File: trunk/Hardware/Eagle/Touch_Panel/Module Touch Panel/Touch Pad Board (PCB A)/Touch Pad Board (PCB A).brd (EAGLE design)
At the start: 140.7 x 94.5 mm, 50 parts, among them U1 SCT2024(CSOG,CSSG,CSTG,CSDG), U2 SCT2024(CSOG,CSSG,CSTG,CSDG), X0 TPTP10R, X1 TPTP10R, X2 TPTP10R, X3 TPTP10R, X4 TPTP10R, Y0 TPTP10R, Y1 TPTP10R, Y2 TPTP10R

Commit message: Work in progress
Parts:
- removed X0, X1, X2, X3, X4, Y0, Y1, Y2: TPTP10R, testpad:TP10R
- moved LED6 77.2 mm to (84.8, 8.99)
- moved LED7 77.0 mm to (109.1, 8.95)
- moved LED12 72.9 mm to (11.9, 59.5), turned to 0 degrees
- moved LED15 72.9 mm to (84.8, 59.5), turned to 0 degrees
- moved LED5 48.6 mm to (60.6, 8.98)
- moved LED4 48.6 mm to (36.2, 9.14)
- moved LED3 34.9 mm to (36.3, 34.0)
- moved LED1 24.9 mm to (11.8, 33.9), turned to 0 degrees
- moved LED2 24.4 mm to (11.8, 9.02)
- moved LED14 24.3 mm to (60.5, 59.5), turned to 0 degrees
- moved LED13 24.3 mm to (36.2, 59.5), turned to 0 degrees
- moved C2 15.6 mm to (58.3, 22.1)
- moved R1 15.0 mm to (58.4, 26.2)
- moved R4 14.1 mm to (58.3, 24.1)
- moved LED26 10.2 mm to (52.1, 20.6)
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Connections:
- removed net N$16: JP2.4, Y1.TP
- removed net N$41: JP2.3, Y0.TP
- removed net N$42: JP3.4, Y2.TP
- removed net N$44: JP4.4, X1.TP
- removed net N$45: JP4.3, X2.TP
- removed net N$46: JP4.2, X0.TP
- removed net N$48: JP5.2, X3.TP
- removed net N$51: JP5.4, X4.TP
- new net X0: JP4.2
- new net X1: JP4.4
- new net X2: JP4.3
- new net X3: JP5.2
- new net X4: JP5.4
- new net Y0: JP2.3
- new net Y1: JP2.4
- new net Y2: JP3.4
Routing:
- net Y2: track 0.00 -> 280.4 mm
- net Y0: track 0.00 -> 279.9 mm
- net Y1: track 0.00 -> 278.8 mm
- net N$29: track 0.00 -> 178.4 mm
- net N$30: track 0.00 -> 150.4 mm
- net N$1: track 0.00 -> 132.5 mm
- net N$31: track 0.00 -> 122.6 mm
- net N$9: track 0.00 -> 109.3 mm
- net N$3: track 0.00 -> 107.1 mm
- net N$2: track 0.00 -> 106.0 mm
- net N$32: track 0.00 -> 94.3 mm
- net N$4: track 0.00 -> 79.3 mm
- net N$8: track 0.00 -> 74.0 mm
- net N$5: track 0.00 -> 52.4 mm
- net N$28: track 0.00 -> 51.7 mm
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- added copper zone on layer 16, net X0
- added copper zone on layer 16, net X1
- added copper zone on layer 16, net X2
- added copper zone on layer 16, net X3
- added copper zone on layer 16, net X4
- removed copper zone on layer 16, net 1B1
- removed copper zone on layer 16, net 1B10
- removed copper zone on layer 16, net 1B11
- removed copper zone on layer 16, net 1B12
- removed copper zone on layer 16, net 1B13
- removed copper zone on layer 16, net 1B14
- removed copper zone on layer 16, net 1B15
- removed copper zone on layer 16, net 1B2
- removed copper zone on layer 16, net 1B3
- removed copper zone on layer 16, net 1B4
- removed copper zone on layer 16, net 1B5
- removed copper zone on layer 16, net 1B6
- removed copper zone on layer 16, net 1B7
- removed copper zone on layer 16, net 1B8
- removed copper zone on layer 16, net 1B9
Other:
- outline, holes or cut-outs redrawn

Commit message: Board of TPB (PCB A) - :)Done
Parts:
- moved JP3 26.6 mm to (71.5, 53.5)
- moved JP2 26.6 mm to (63.7, 28.2)
- moved D1 3.30 mm to (84.8, 53.3), turned to 270 degrees
- moved C2 2.10 mm to (58.3, 24.2)
- moved R4 1.98 mm to (58.3, 22.1)
- moved JP4 0.80 mm to (63.8, 53.5)
- moved JP1 0.16 mm to (80.7, 41.4)
- turned LED10 to 180 degrees
- turned LED5 to 180 degrees
- turned LED8 to 180 degrees
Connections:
- net GND: now also JP2.3, JP2.4, JP3.2; no longer JP2.1, JP2.2, JP3.3
- net Y0: now also JP2.2; no longer JP2.3
- net Y1: now also JP2.1; no longer JP2.4
- net Y2: now also JP3.3; no longer JP3.4
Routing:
- net LED_DP: track 0.00 -> 386.7 mm, vias 0 -> 21
- net +3V3: track 0.00 -> 114.4 mm, vias 0 -> 9
- net GND: track 11.4 -> 110.2 mm, vias 0 -> 7
- net N$36: track 0.00 -> 62.2 mm, vias 0 -> 3
- net N$35: track 0.00 -> 61.7 mm, vias 0 -> 3
- net N$34: track 10.7 -> 69.8 mm, vias 0 -> 4
- net X4: track 40.0 -> 94.6 mm
- net N$8: track 74.0 -> 25.8 mm, vias 0 -> 2
- net X0: track 34.0 -> 78.0 mm, vias 0 -> 2
- net X1: track 35.9 -> 68.5 mm
- net Y0: track 279.9 -> 308.8 mm, vias 0 -> 1
- net N$37: track 0.00 -> 19.9 mm, vias 0 -> 2
- net X3: track 34.4 -> 50.8 mm
- net 1: track 16.1 -> 0.00 mm
- net N$5: track 52.4 -> 44.4 mm
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- added copper zone on layer 1, net N$14
- removed copper zone on layer 16, net 1B
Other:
- board size 140.7 x 94.5 mm -> 142.3 x 82 mm
- board text added: "Touch Pad Board (PCB A) ver. 1.00"

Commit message: Work in progress
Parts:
- added R5: 10, resistor:R0805
- added U$1: PHOTO_TRANS, myHome:PHOTO_TRANS
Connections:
- new net N$15: JP3.1, R5.2, U$1.C
- net +3V3: now also U$1.A
- net GND: now also R5.1; no longer JP3.1
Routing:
- net X2: track 37.0 -> 51.7 mm
- net +3V3: track 114.4 -> 123.1 mm, vias 9 -> 10
- net N$15: track 0.00 -> 7.02 mm
- net GND: track 110.2 -> 107.4 mm
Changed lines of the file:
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@@
 <layer number="17" name="Pads" color="2" fill="1" visible="yes" active="yes"/>
 <layer number="18" name="Vias" color="2" fill="1" visible="yes" active="yes"/>
-<layer number="19" name="Unrouted" color="6" fill="1" visible="no" active="yes"/>
-<layer number="20" name="Dimension" color="15" fill="1" visible="yes" active="yes"/>
+<layer number="19" name="Unrouted" color="6" fill="1" visible="yes" active="yes"/>
+<layer number="20" name="Dimension" color="15" fill="1" visible="no" active="yes"/>
 <layer number="21" name="tPlace" color="7" fill="1" visible="no" active="yes"/>
 <layer number="22" name="bPlace" color="7" fill="1" visible="no" active="yes"/>
 <layer number="23" name="tOrigins" color="15" fill="1" visible="no" active="yes"/>
 <layer number="24" name="bOrigins" color="15" fill="1" visible="no" active="yes"/>
-<layer number="25" name="tNames" color="7" fill="1" visible="yes" active="yes"/>
-<layer number="26" name="bNames" color="7" fill="1" visible="yes" active="yes"/>
+<layer number="25" name="tNames" color="7" fill="1" visible="no" active="yes"/>
+<layer number="26" name="bNames" color="7" fill="1" visible="no" active="yes"/>
 <layer number="27" name="tValues" color="7" fill="1" visible="no" active="yes"/>
 <layer number="28" name="bValues" color="7" fill="1" visible="no" active="yes"/>
@@
 <layer number="37" name="tTest" color="7" fill="1" visible="no" active="yes"/>
 <layer number="38" name="bTest" color="7" fill="1" visible="no" active="yes"/>
-<layer number="39" name="tKeepout" color="4" fill="11" visible="no" active="yes"/>
-<layer number="40" name="bKeepout" color="1" fill="11" visible="no" active="yes"/>
-<layer number="41" name="tRestrict" color="4" fill="10" visible="no" active="yes"/>
-<layer number="42" name="bRestrict" color="1" fill="10" visible="no" active="yes"/>
+<layer number="39" name="tKeepout" color="4" fill="11" visible="yes" active="yes"/>
+<layer number="40" name="bKeepout" color="1" fill="11" visible="yes" active="yes"/>
+<layer number="41" name="tRestrict" color="4" fill="10" visible="yes" active="yes"/>
+<layer number="42" name="bRestrict" color="1" fill="10" visible="yes" active="yes"/>
 <layer number="43" name="vRestrict" color="2" fill="10" visible="no" active="yes"/>
 <layer number="44" name="Drills" color="7" fill="1" visible="no" active="yes"/>
-<layer number="45" name="Holes" color="7" fill="1" visible="yes" active="yes"/>
+<layer number="45" name="Holes" color="7" fill="1" visible="no" active="yes"/>
 <layer number="46" name="Milling" color="3" fill="1" visible="no" active="yes"/>
 <layer number="47" name="Measures" color="7" fill="1" visible="no" active="yes"/>
@@
 <rectangle x1="98.38" y1="13.61" x2="111.87" y2="18.01" layer="41"/>
 <rectangle x1="73.96" y1="38.65" x2="87.45" y2="43.05" layer="41"/>
-<rectangle x1="57.84" y1="17.29" x2="71.33" y2="21.69" layer="41" rot="R90"/>
+<rectangle x1="57.84" y1="18.19" x2="71.33" y2="22.59" layer="41" rot="R90"/>
 <rectangle x1="57.63" y1="34.56" x2="71.12" y2="38.96" layer="41" rot="R90"/>
-<rectangle x1="65.83" y1="59.96" x2="79.32" y2="64.36" layer="41" rot="R90"/>
+<rectangle x1="65.93" y1="58.66" x2="79.42" y2="63.06" layer="41" rot="R90"/>
 <text x="130.5" y="2.55" size="1.778" layer="16" rot="MR0">Touch Pad Board (PCB A) ver. 1.00</text>
 <rectangle x1="25.44" y1="64.32" x2="38.93" y2="68.72" layer="42"/>
 <text x="91.44" y="2.54" size="1.778" layer="25">Touch Pad Board (PCB A) ver. 1.00</text>
 <text x="91.54" y="4.26" size="1.778" layer="26" rot="MR180">Touch Pad Board (PCB A) ver. 1.00</text>
-<hole x="77.47" y="53.34" drill="0.6"/>
 </plain>
 <attributes>
@@
 <element name="JP5" library="pinhead" package="2X2SMD" value="" x="73.54" y="28.18" locked="yes" rot="MR0"/>
 <element name="JP1" library="pinhead" package="2X3SMD" value="" x="80.72" y="41.41" locked="yes" rot="MR90"/>
+<element name="U$1" library="myHome" package="PHOTO_TRANS" value="PHOTO_TRANS" x="68.57" y="54.01" rot="MR180"/>
+<element name="R5" library="resistor" package="R0805" value="10" x="68.66" y="50.43" rot="MR90"/>
 </elements>
 <signals>
@@
 <contactref element="C2" pad="1"/>
 <contactref element="C1" pad="1"/>
-<contactref element="JP3" pad="1"/>
 <contactref element="JP1" pad="P1"/>
 <wire x1="54.15" y1="26.2225" x2="55.3225" y2="26.2225" width="0.3048" layer="16"/>
@@
 <wire x1="65.615" y1="25.65" x2="65.615" y2="23.015" width="0.6096" layer="16"/>
 <wire x1="65.615" y1="23.015" x2="65.4" y2="22.8" width="0.6096" layer="16"/>
-<wire x1="70.915" y1="56.06" x2="70.915" y2="50.98" width="0.6096" layer="16"/>
 <wire x1="77.545" y1="38.235" x2="77.51" y2="38.2" width="0.6096" layer="16"/>
 <wire x1="77.51" y1="38.2" x2="76.2" y2="38.2" width="0.6096" layer="16"/>
@@
 <wire x1="75" y1="48.3" x2="71.2" y2="48.3" width="0.6096" layer="16"/>
 <wire x1="71.2" y1="48.3" x2="71" y2="48.5" width="0.6096" layer="16"/>
-<wire x1="71" y1="48.5" x2="71" y2="50.68" width="0.6096" layer="16"/>
+<wire x1="71" y1="48.5" x2="71" y2="49.6" width="0.6096" layer="16"/>
+<wire x1="71" y1="49.6" x2="71" y2="50.68" width="0.6096" layer="16"/>
 <wire x1="71" y1="50.68" x2="71.12" y2="50.8" width="0.6096" layer="16"/>
 <wire x1="71.12" y1="50.8" x2="71" y2="50.8" width="0.6096" layer="16"/>
@@
 <wire x1="60.84" y1="24.16" x2="62.2" y2="22.8" width="0.6096" layer="16"/>
 <wire x1="62.2" y1="22.8" x2="65.4" y2="22.8" width="0.6096" layer="16"/>
+<contactref element="R5" pad="1"/>
+<wire x1="68.66" y1="49.58" x2="70.98" y2="49.58" width="0.6096" layer="16"/>
+<wire x1="70.98" y1="49.58" x2="71" y2="49.6" width="0.6096" layer="16"/>
 </signal>
 <signal name="+3V3">
@@
 <wire x1="61" y1="48.1" x2="65.6" y2="48.1" width="0.6096" layer="16"/>
 <via x="65.6" y="48.1" extent="1-16" drill="0.4"/>
-<wire x1="65.6" y1="48.1" x2="85.4" y2="48.1" width="0.6096" layer="1"/>
+<wire x1="65.6" y1="48.1" x2="68.58" y2="48.1" width="0.6096" layer="1"/>
+<wire x1="68.58" y1="48.1" x2="85.4" y2="48.1" width="0.6096" layer="1"/>
 <wire x1="85.4" y1="48.1" x2="85.7" y2="48.4" width="0.6096" layer="1"/>
+<contactref element="U$1" pad="A"/>
+<wire x1="68.57" y1="55.06" x2="68.57" y2="55.87" width="0.6096" layer="16"/>
+<wire x1="68.57" y1="55.87" x2="68.6" y2="55.9" width="0.6096" layer="16"/>
+<via x="68.6" y="55.9" extent="1-16" drill="0.5"/>
+<wire x1="68.6" y1="55.9" x2="68.6" y2="48.12" width="0.6096" layer="1"/>
+<wire x1="68.6" y1="48.12" x2="68.58" y2="48.1" width="0.6096" layer="1"/>
 </signal>
 <signal name="N$25">
@@
 <vertex x="62.5" y="34.9"/>
 </polygon>
-<wire x1="67.5" y1="45.03" x2="67.5" y2="56.1" width="0.3048" layer="16"/>
 <polygon width="0.4064" layer="16">
 <vertex x="62.5" y="72.2"/>
@@
 </polygon>
 <contactref element="JP4" pad="3"/>
-<wire x1="67.5" y1="56.1" x2="67.5" y2="56.2" width="0.3048" layer="16"/>
-<wire x1="67.5" y1="56.2" x2="67.5" y2="61.83" width="0.3048" layer="16"/>
+<wire x1="66.2" y1="56.03" x2="67.5" y2="56" width="0.3048" layer="16"/>
+<wire x1="67.5" y1="56" x2="67.5" y2="56.1" width="0.3048" layer="16"/>
+<wire x1="67.5" y1="56.1" x2="67.5" y2="56" width="0.3048" layer="16"/>
+<wire x1="67.5" y1="56" x2="66.2" y2="56.03" width="0.3048" layer="16"/>
+<wire x1="67.5" y1="56.1" x2="67.5" y2="61.83" width="0.3048" layer="16"/>
 <wire x1="67.5" y1="61.83" x2="67.03" y2="61.73" width="0.254" layer="16"/>
 <wire x1="65.715" y1="56.06" x2="67.46" y2="56.06" width="0.254" layer="16"/>
 <wire x1="67.46" y1="56.06" x2="67.5" y2="56.1" width="0.254" layer="16"/>
+<wire x1="66.2" y1="56.03" x2="67.5" y2="56" width="0.3048" layer="16"/>
+<wire x1="67.5" y1="56" x2="67" y2="56" width="0.3048" layer="16"/>
+<wire x1="67" y1="56" x2="67" y2="52.3" width="0.3048" layer="16"/>
+<wire x1="67" y1="52.3" x2="67.2" y2="51.2" width="0.3048" layer="16"/>
+<wire x1="67.2" y1="51.2" x2="67.2" y2="44.5" width="0.3048" layer="16"/>
+<wire x1="67.5" y1="56.1" x2="65.8" y2="56.1" width="0.3048" layer="16"/>
+<wire x1="65.8" y1="56.1" x2="65.7" y2="56" width="0.3048" layer="16"/>
+<wire x1="67.5" y1="45.03" x2="67.5" y2="38.5" width="0.3048" layer="16"/>
+<wire x1="67.5" y1="38.5" x2="68.4" y2="37.6" width="0.3048" layer="16"/>
 </signal>
 <signal name="N$14">
@@
 </polygon>
 </signal>
+<signal name="N$15">
+<contactref element="U$1" pad="C"/>
+<contactref element="R5" pad="2"/>
+<contactref element="JP3" pad="1"/>
+<wire x1="68.66" y1="51.28" x2="68.66" y2="52.87" width="0.6096" layer="16"/>
+<wire x1="68.66" y1="52.87" x2="68.57" y2="52.96" width="0.6096" layer="16"/>
+<wire x1="68.57" y1="52.96" x2="68.74" y2="52.96" width="0.6096" layer="16"/>
+<wire x1="68.74" y1="52.96" x2="69.1" y2="52.6" width="0.6096" layer="16"/>
+<wire x1="69.1" y1="52.6" x2="69.8" y2="52.6" width="0.6096" layer="16"/>
+<wire x1="69.8" y1="52.6" x2="69.8" y2="52.7" width="0.6096" layer="16"/>
+<wire x1="69.8" y1="52.7" x2="70.9" y2="53.8" width="0.6096" layer="16"/>
+<wire x1="70.9" y1="53.8" x2="70.9" y2="56.045" width="0.6096" layer="16"/>
+<wire x1="70.9" y1="56.045" x2="70.915" y2="56.06" width="0.6096" layer="16"/>
+</signal>
 </signals>

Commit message: Work in progress
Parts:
- R5: value 10 -> 4k6
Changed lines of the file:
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@@
 <element name="JP1" library="pinhead" package="2X3SMD" value="" x="80.72" y="41.41" locked="yes" rot="MR90"/>
 <element name="U$1" library="myHome" package="PHOTO_TRANS" value="PHOTO_TRANS" x="68.57" y="54.01" rot="MR180"/>
-<element name="R5" library="resistor" package="R0805" value="10" x="68.66" y="50.43" rot="MR90"/>
+<element name="R5" library="resistor" package="R0805" value="4k6" x="68.66" y="50.43" rot="MR90"/>
 </elements>
 <signals>

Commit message: Touch Panel PCB_A & PCB_B final version (to electrical&part check)
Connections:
- net N$15 renamed OPTO
- removed net X3: JP5.2
- new net X5: JP5.4
- net N$34: no longer JP1.P3
- net X4: now also JP5.2; no longer JP5.4
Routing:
- net X5: track 0.00 -> 94.6 mm
- net X3: track 50.8 -> 0.00 mm, vias 2 -> 0
- net X4: track 94.6 -> 50.8 mm, vias 0 -> 2
- net N$34: track 69.8 -> 47.3 mm, vias 4 -> 2
- net N$3: track 107.1 -> 105.5 mm
- net N$5: track 44.4 -> 42.9 mm
- net N$2: track 106.0 -> 104.6 mm
- net N$4: track 79.3 -> 77.9 mm
- net LED_DP: track 386.7 -> 388.0 mm
- net N$1: track 132.5 -> 131.5 mm
- added copper zone on layer 16, net X5
- removed copper zone on layer 16, net X3

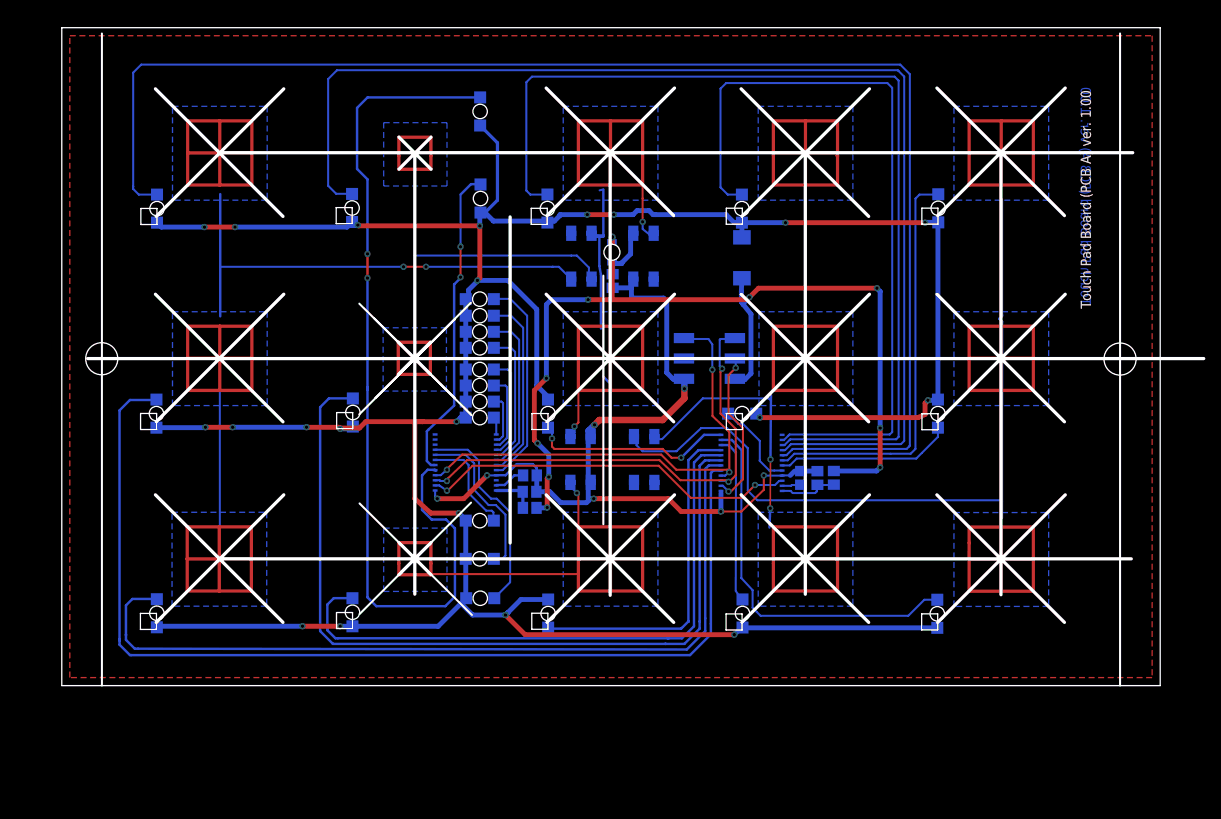
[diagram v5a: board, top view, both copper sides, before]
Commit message: Touch Panel (PCBA+PCBB) ver. 1.00
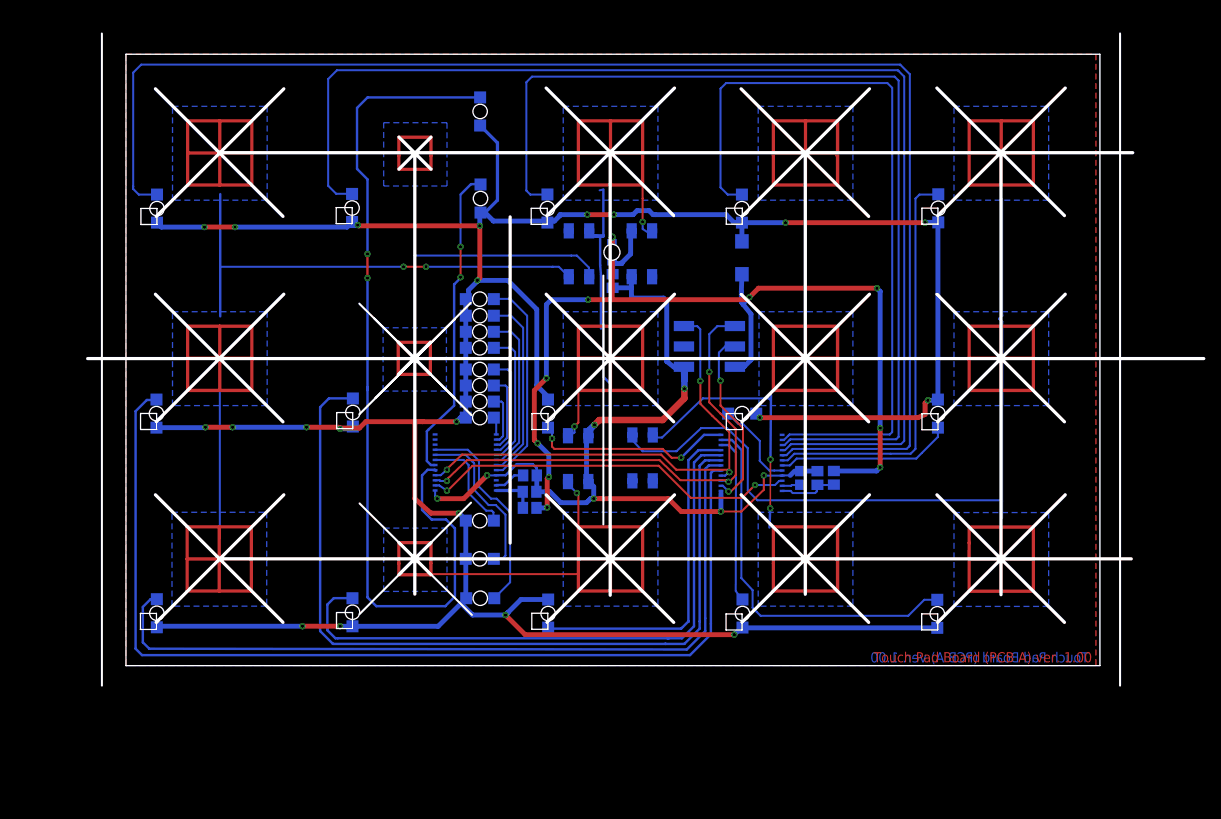
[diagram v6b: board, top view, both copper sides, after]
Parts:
- D1: device diode:DO214AA -> diode:DO214AC
- moved JP1 1.50 mm to (80.7, 42.9)
- moved JP4 0.42 mm to (63.5, 53.8)
- moved JP3 0.36 mm to (71.3, 53.8)
- moved JP2 0.32 mm to (63.4, 28.3)
- moved JP5 0.28 mm to (73.3, 28.4)
- renumbered U$1 to SFH3710
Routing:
- net N$2: track 104.6 -> 100.3 mm
- net N$1: track 131.5 -> 127.8 mm
- net N$37: track 19.9 -> 23.0 mm
- net N$36: track 62.2 -> 64.7 mm
- net GND: track 107.4 -> 109.6 mm
- net +3V3: track 123.1 -> 121.9 mm
- net N$35: track 61.7 -> 62.7 mm
- net LED_DP: track 388.0 -> 388.5 mm
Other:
- board size 142.3 x 82 mm -> 139.1 x 81.3 mm
